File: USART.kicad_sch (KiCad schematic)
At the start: 60 parts, among them X1 USART TTL, X2 Conn_01x10, X3 Power, X4 Address, X5 Data, X6 Mode, X7 Control, X8 Clock

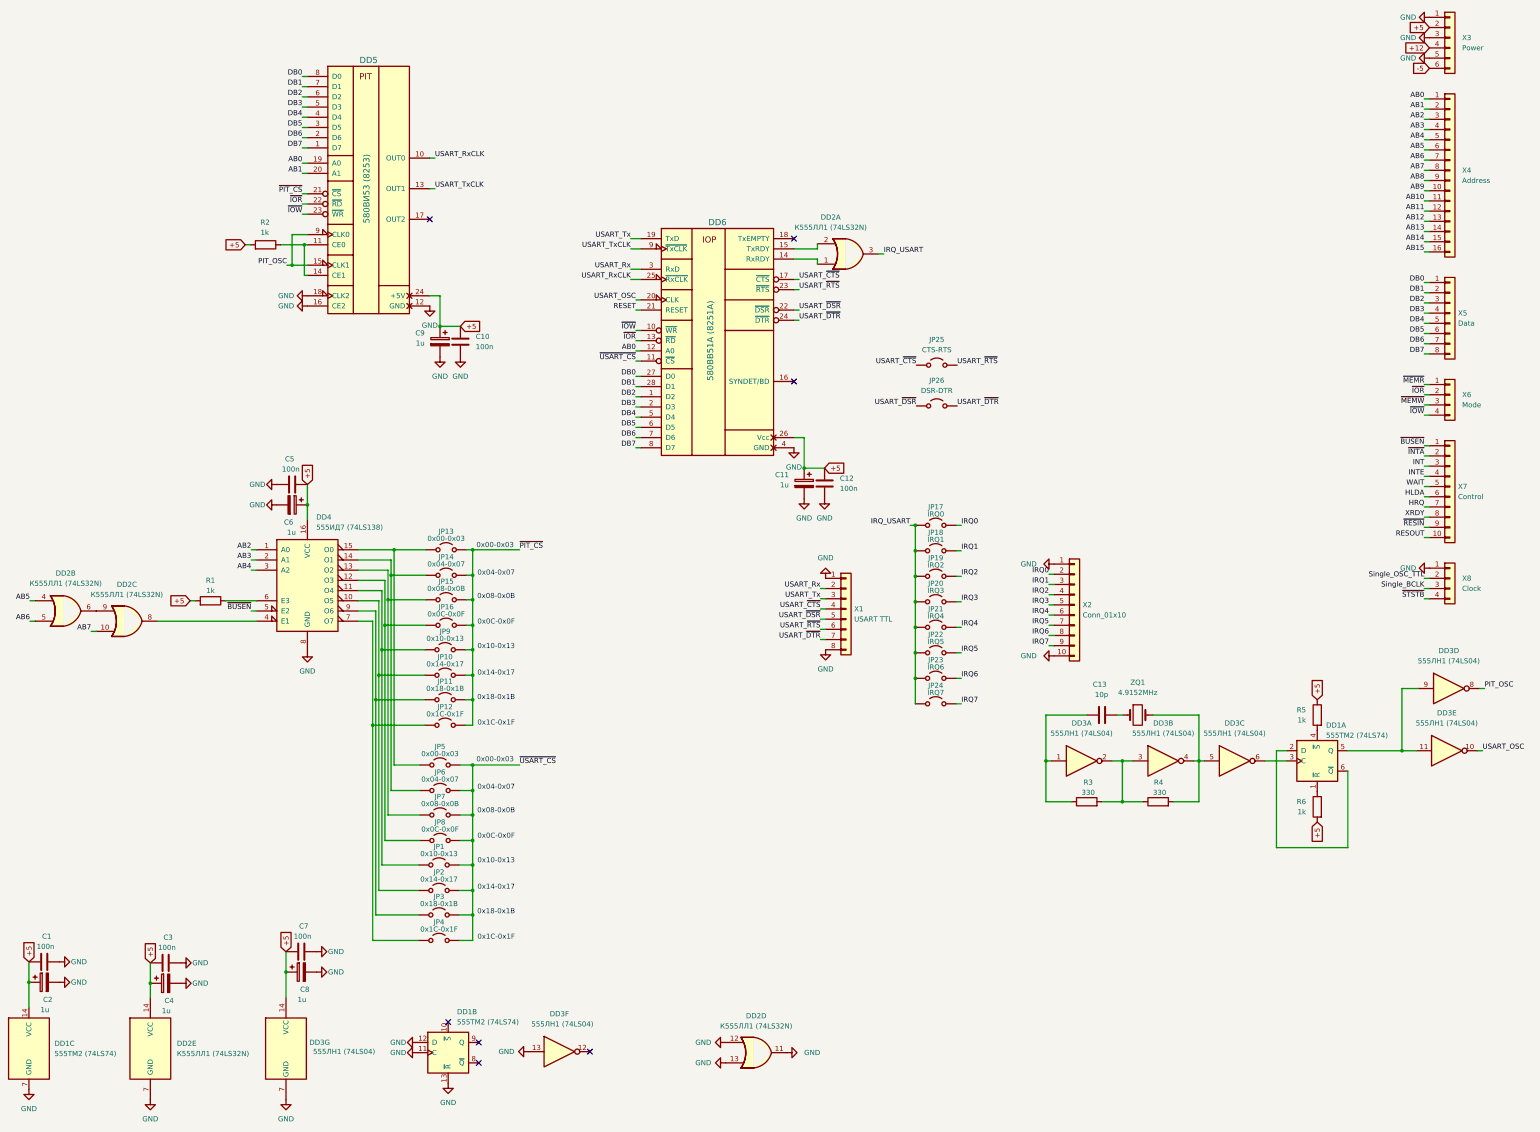
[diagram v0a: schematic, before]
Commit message: Update+fix
- Replaced the standard logic oscillator with a monolithic quartz oscillator;
- Fixed the 'CLK' source of the 580VV51 (8251);
- Connected the reset signal of the 580VV51 (8251).

- Заменен генератор на стандартной логике на монолитный кварцевый генератор;
- Исправлен источник 'CLK' у 580ВВ51 (8251);
- Подключен сигнал сброса у 580ВВ51 (8251).
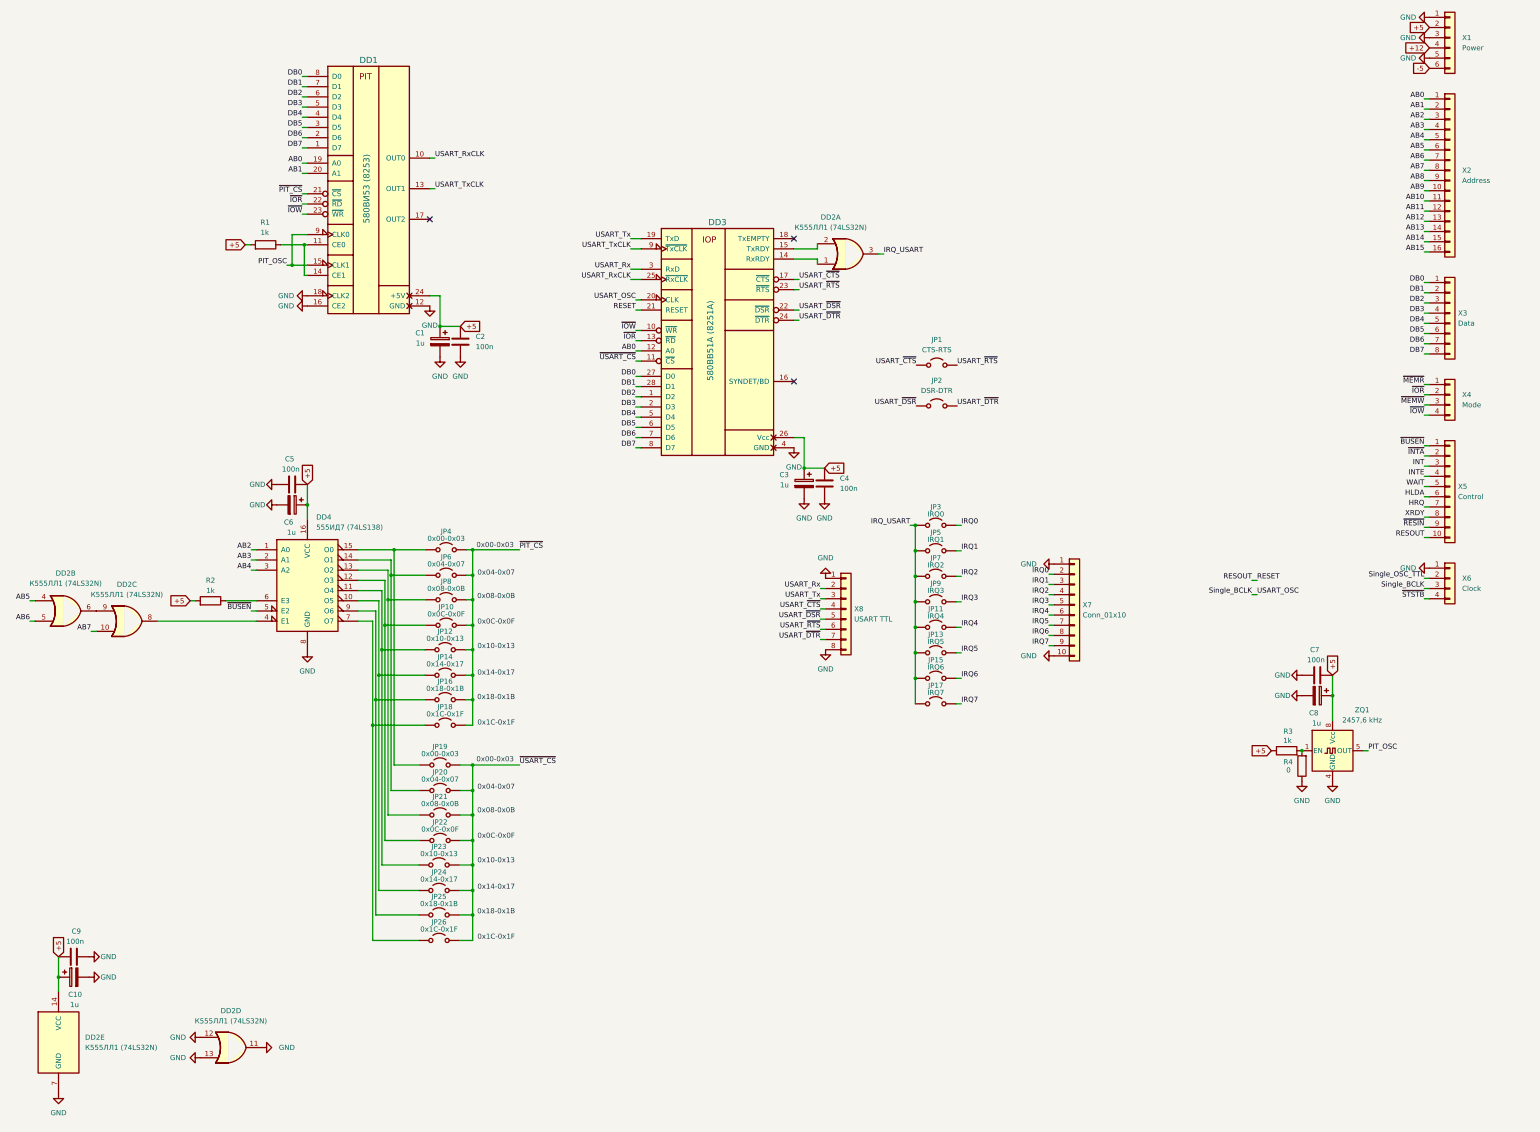
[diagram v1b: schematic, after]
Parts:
- removed C1: 100n, Capacitor_SMD:C_0805_2012Metric_Pad1.18x1.45mm_HandSolder, symbol Device:C
- removed C13: 10p, Capacitor_SMD:C_0805_2012Metric_Pad1.18x1.45mm_HandSolder, symbol Device:C
- removed C2: 1u, Capacitor_Tantalum_SMD:CP_EIA-3216-18_Kemet-A_Pad1.58x1.35mm_HandSolder, symbol Device:C_Polarized
- removed DD1: 555ТМ2 (74LS74), Package_DIP:DIP-14_W7.62mm_Socket_LongPads, symbol 74xx:74LS74
- removed DD3: 555ЛН1 (74LS04), Package_DIP:DIP-14_W7.62mm_Socket_LongPads, symbol 74xx:74LS04
- removed R5, R6: 1k, Resistor_SMD:R_0805_2012Metric_Pad1.20x1.40mm_HandSolder, symbol Device:R
- removed ZQ1: 4.9152MHz, Crystal:Crystal_HC49-U_Vertical, symbol Device:Crystal
- added ZQ1: 2457,6 kHz, Oscillator:Oscillator_DIP-8_LargePads, symbol Oscillator:CXO_DIP8
- R3: value 330 -> 1k
- R4: value 330 -> 0
- renumbered C9 to C1, C4 to C10, C10 to C2, C11 to C3, C12 to C4, C3 to C9, DD5 to DD1, DD6 to DD3, JP25 to JP1, JP16 to JP10, JP21 to JP11, JP9 to JP12, JP22 to JP13, JP10 to JP14, JP23 to JP15, JP11 to JP16, JP24 to JP17, JP12 to JP18, JP5 to JP19, JP26 to JP2, JP6 to JP20, JP7 to JP21, JP8 to JP22, JP1 to JP23, JP2 to JP24, JP3 to JP25, JP4 to JP26, JP17 to JP3, JP13 to JP4, JP18 to JP5, JP14 to JP6, JP19 to JP7, JP15 to JP8, JP20 to JP9, R2 to R1, R1 to R2, X3 to X1, X4 to X2, X5 to X3, X6 to X4, X7 to X5, X8 to X6, X2 to X7, X1 to X8
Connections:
- net RESOUT is gone; now on net RESET: X5.10 (Pin_10)
- net USART_OSC is gone; now on net Single_BCLK: DD3.20 (CLK)
- net +5: now also R3.1, ZQ1.8 (Vcc)
- net GND: now also R4.1, ZQ1.4 (GND)
- net PIT_OSC: now also ZQ1.5 (OUT)
- net at R4.2: now also R3.2, ZQ1.1 (EN)
- no-connect marks 7 -> 3
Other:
- moved on the sheet: C10, C9, DD2D, DD2E

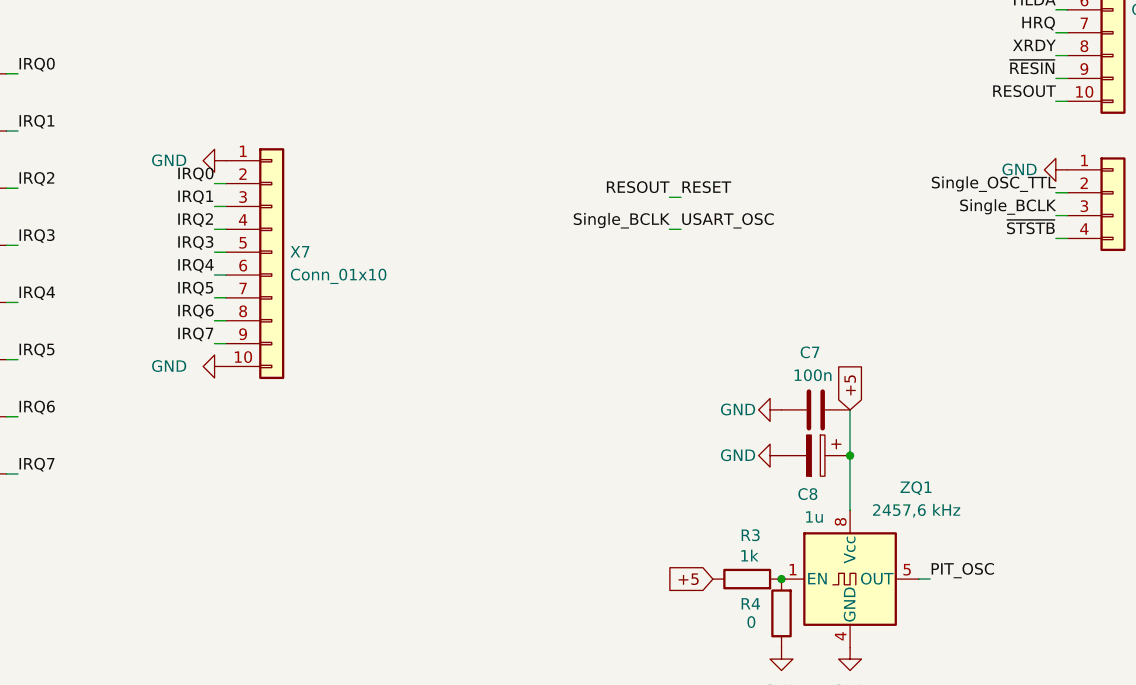
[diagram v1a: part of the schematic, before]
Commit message: Add files via upload
Changed IRQ bus pin's

Изменены пины шины IRQ
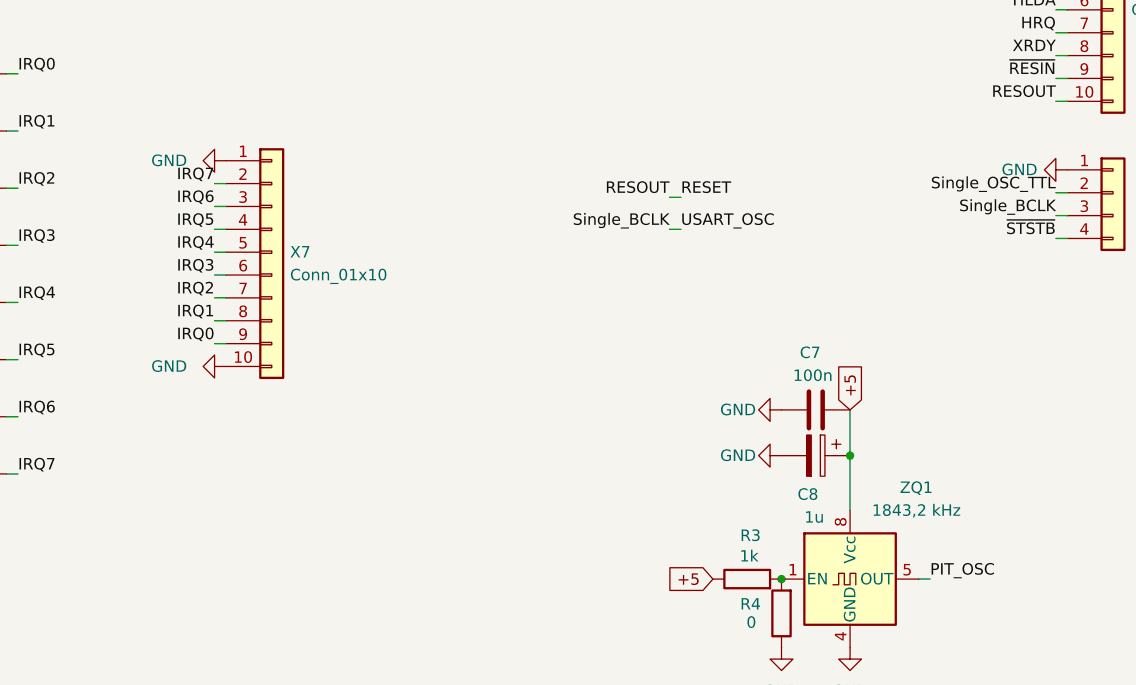
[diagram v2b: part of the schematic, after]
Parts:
- ZQ1: value 2457,6 kHz -> 1843,2 kHz
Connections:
- net IRQ0: now also X7.9 (Pin_9); no longer X7.2 (Pin_2)
- net IRQ1: now also X7.8 (Pin_8); no longer X7.3 (Pin_3)
- net IRQ2: now also X7.7 (Pin_7); no longer X7.4 (Pin_4)
- net IRQ3: now also X7.6 (Pin_6); no longer X7.5 (Pin_5)
- net IRQ4: now also X7.5 (Pin_5); no longer X7.6 (Pin_6)
- net IRQ5: now also X7.4 (Pin_4); no longer X7.7 (Pin_7)
- net IRQ6: now also X7.3 (Pin_3); no longer X7.8 (Pin_8)
- net IRQ7: now also X7.2 (Pin_2); no longer X7.9 (Pin_9)
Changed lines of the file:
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@@
 	)
 	(label "IRQ1"
-		(at 282.956 157.226 180)
+		(at 282.956 169.926 180)
 		(effects
 			(font
@@
 	)
 	(label "IRQ6"
-		(at 282.956 169.926 180)
+		(at 282.956 157.226 180)
 		(effects
 			(font
@@
 	)
 	(label "IRQ2"
-		(at 282.956 159.766 180)
+		(at 282.956 167.386 180)
 		(effects
 			(font
@@
 	)
 	(label "IRQ3"
-		(at 282.956 162.306 180)
+		(at 282.956 164.846 180)
 		(effects
 			(font
@@
 	)
 	(label "IRQ4"
-		(at 282.956 164.846 180)
+		(at 282.956 162.306 180)
 		(effects
 			(font
@@
 	)
 	(label "IRQ7"
-		(at 282.956 172.466 180)
+		(at 282.956 154.686 180)
 		(effects
 			(font
@@
 	)
 	(label "IRQ5"
-		(at 282.956 167.386 180)
+		(at 282.956 159.766 180)
 		(effects
 			(font
@@
 	)
 	(label "IRQ0"
-		(at 282.956 154.686 180)
+		(at 282.956 172.466 180)
 		(effects
 			(font
@@
 				)
 			)
+			(project "K580"
+				(path "/d39f0047-e7e5-4cec-bc5c-1058f4d3a193/32ee06fd-3e97-45bf-b93e-6643f1e6a498"
+					(reference "C?")
+					(unit 1)
+				)
+			)
 		)
 	)
@@
 				)
 			)
+			(project "K580"
+				(path "/d39f0047-e7e5-4cec-bc5c-1058f4d3a193/32ee06fd-3e97-45bf-b93e-6643f1e6a498"
+					(reference "#PWR?")
+					(unit 1)
+				)
+			)
 		)
 	)
@@
 				)
 			)
+			(project "K580"
+				(path "/d39f0047-e7e5-4cec-bc5c-1058f4d3a193/32ee06fd-3e97-45bf-b93e-6643f1e6a498"
+					(reference "#PWR?")
+					(unit 1)
+				)
+			)
 		)
 	)
@@
 				)
 			)
+			(project "K580"
+				(path "/d39f0047-e7e5-4cec-bc5c-1058f4d3a193/32ee06fd-3e97-45bf-b93e-6643f1e6a498"
+					(reference "C?")
+					(unit 1)
+				)
+			)
 		)
 	)
@@
 				)
 			)
+			(project "K580"
+				(path "/d39f0047-e7e5-4cec-bc5c-1058f4d3a193/32ee06fd-3e97-45bf-b93e-6643f1e6a498"
+					(reference "R?")
+					(unit 1)
+				)
+			)
 		)
 	)
@@
 				)
 			)
+			(project "K580"
+				(path "/d39f0047-e7e5-4cec-bc5c-1058f4d3a193/32ee06fd-3e97-45bf-b93e-6643f1e6a498"
+					(reference "R?")
+					(unit 1)
+				)
+			)
 		)
 	)
@@
 				)
 			)
+			(project "K580"
+				(path "/d39f0047-e7e5-4cec-bc5c-1058f4d3a193/32ee06fd-3e97-45bf-b93e-6643f1e6a498"
+					(reference "#PWR?")
+					(unit 1)
+				)
+			)
 		)
 	)
@@
 				)
 			)
+			(project "K580"
+				(path "/d39f0047-e7e5-4cec-bc5c-1058f4d3a193/32ee06fd-3e97-45bf-b93e-6643f1e6a498"
+					(reference "#PWR?")
+					(unit 1)
+				)
+			)
 		)
 	)
@@
 			)
 		)
-		(property "Value" "2457,6 kHz"
+		(property "Value" "1843,2 kHz"
 			(at 360.934 191.008 0)
 			(effects
@@
 					(unit 1)
 				)
+			)
+			(project "K580"
+				(path "/d39f0047-e7e5-4cec-bc5c-1058f4d3a193/32ee06fd-3e97-45bf-b93e-6643f1e6a498"
+					(reference "ZQ?")
+					(unit 1)
+				)

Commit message: Add files via upload
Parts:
- added C7: 100n, Capacitor_SMD:C_0805_2012Metric_Pad1.18x1.45mm_HandSolder, symbol Device:C
- renumbered C9 to C10, C10 to C11, C7 to C8, C8 to C9, JP11 to JP10, JP10 to JP11, JP13 to JP12, JP12 to JP13, JP15 to JP14, JP14 to JP15, JP17 to JP16, JP16 to JP17, JP5 to JP4, JP4 to JP5, JP7 to JP6, JP6 to JP7, JP9 to JP8, JP8 to JP9
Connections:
- net GND: now also C7.2
- net at DD4.6 (E3), R2.1: now also C7.1
- net INTE renamed ~{WRQ}
- net RESET renamed RESOUT
- net Single_BCLK renamed F2TTL
- net Single_OSC_TTL renamed OSC_TTL
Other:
- moved on the sheet: C5, C6, DD2B, DD2C, DD4, JP11, JP13, JP15, JP17, JP18, JP19, JP20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
